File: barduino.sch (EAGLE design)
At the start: 30 parts, among them J1 JACK.65MM, Q2 16MHz

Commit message: Stripped a lot and added some clock parts
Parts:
- removed FTDI: (no value), pinhead:PINHD-1X6
- removed JP1, JP2: (no value), SparkFun:M04PTH
- removed JP3: (no value), SparkFun:M06LOCK
- removed JP4, JP5: (no value), SparkFun:M02LOCK
- removed R5: 0, ng:RESISTOR1206
- removed SCHOTTKY_2: (no value), 01_ng:DIODESOD123
- added LED1: (no value), microbuilder:DISP_SEGMENT_4DIGIT_BL-Q56C43
- added SG1: F/CM12P, buzzer:F/CM12P
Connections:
- removed net CONNECT: FTDI.3, SCHOTTKY_2.A
- new net N$22: LED1.P$6
- new net N$23: LED1.P$7
- new net N$27: LED1.P$11
- net A0: no longer JP1.4
- net A1: no longer JP1.3
- net A2: no longer JP1.2
- net A3: no longer JP1.1
- net D0: now also LED1.P$12; no longer FTDI.4, JP2.4
- net D1: now also LED1.P$8; no longer FTDI.5, JP2.3
- net D10: now also SG1.1; no longer JP3.1
- net D2: now also LED1.P$13; no longer JP2.2
- net D3: now also LED1.P$9; no longer JP2.1
- net D4: now also LED1.P$10
- net D5: no longer JP3.6
- net D6: no longer JP3.5
- net D7: no longer JP3.4
- net D8: no longer JP3.3
- net D9: no longer JP3.2
- net GND: now also SG1.2; no longer FTDI.1, JP4.2, JP5.2
- net RTS#: no longer FTDI.6
- net VCC: no longer JP4.1, JP5.1, SCHOTTKY_2.C
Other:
- note added: "Buzzer"
- moved on the sheet: ICSP

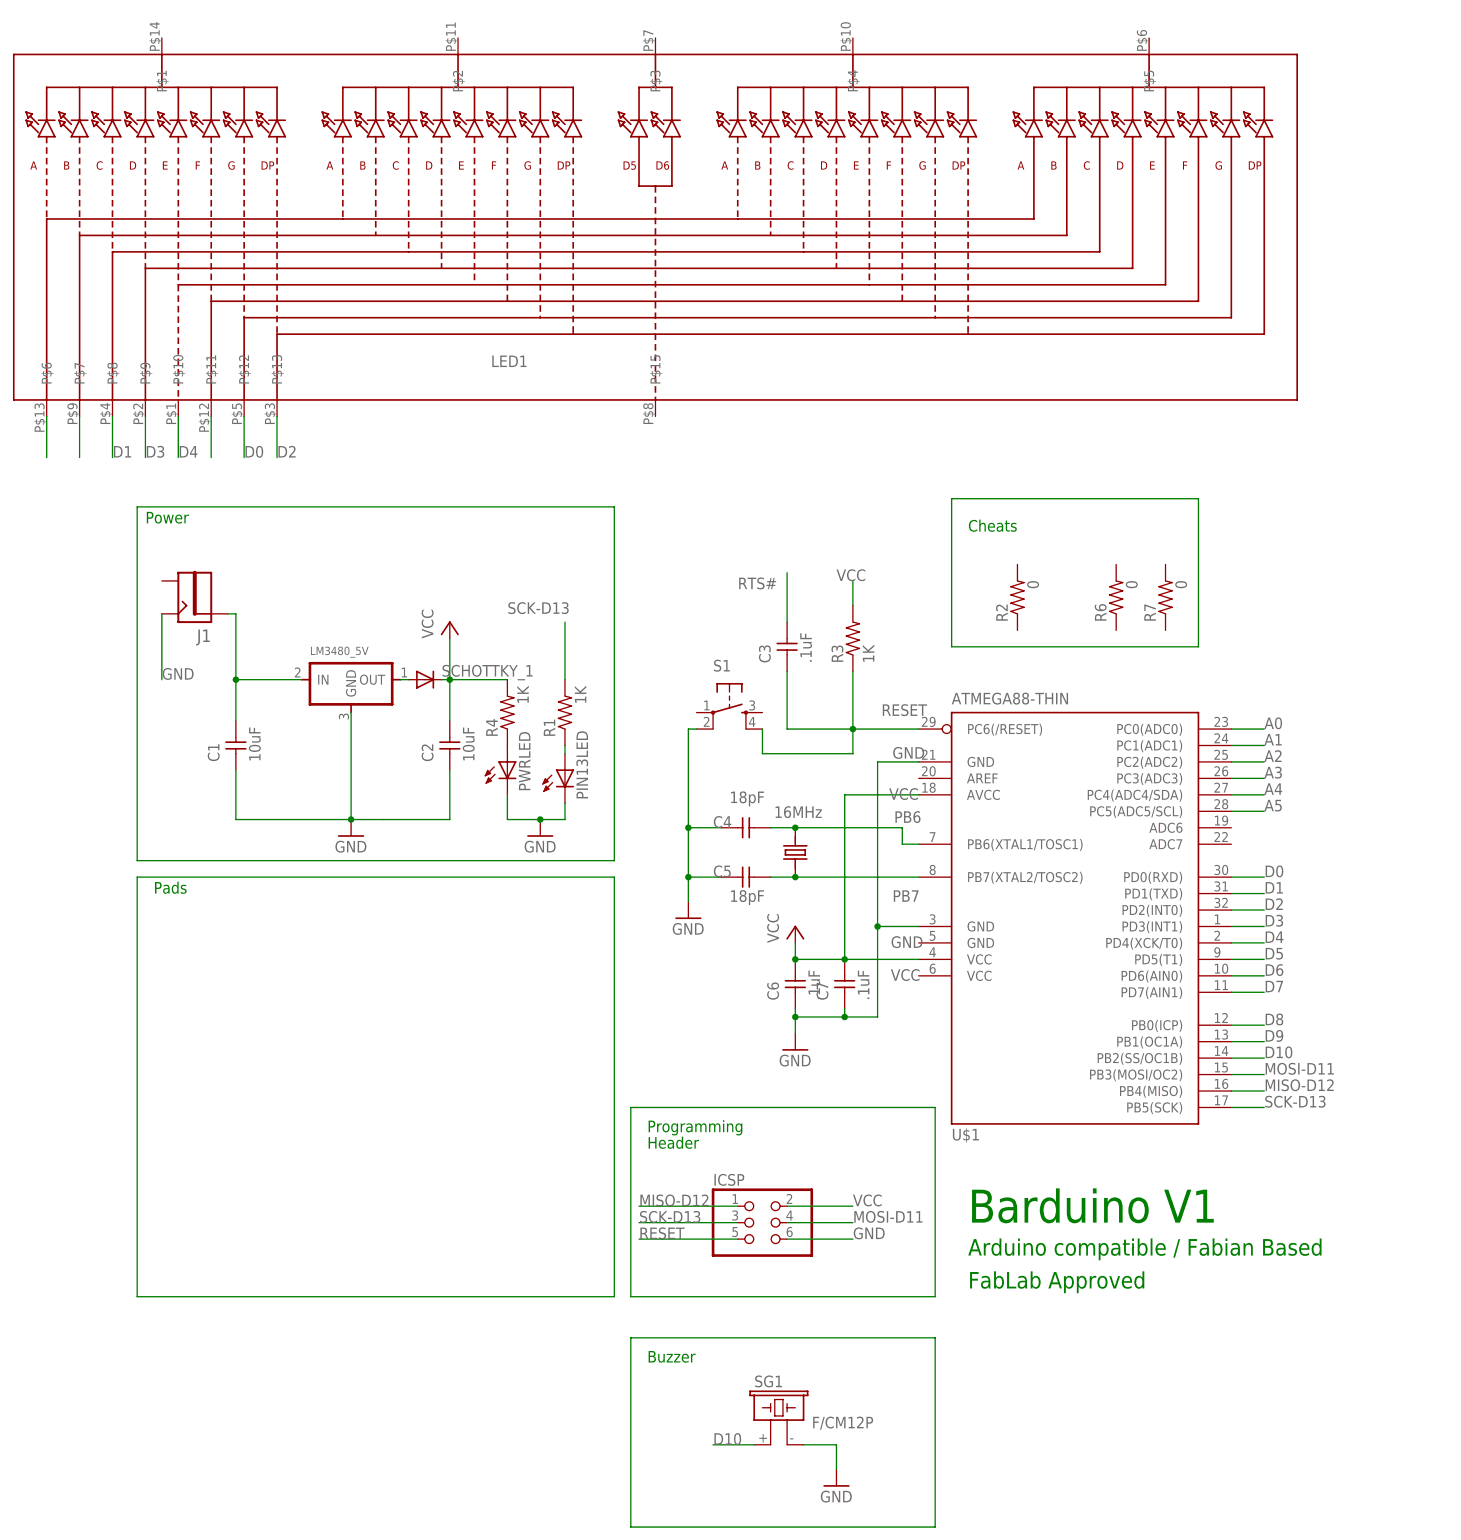
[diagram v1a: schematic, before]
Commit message: Replace pwr jack with usb conn
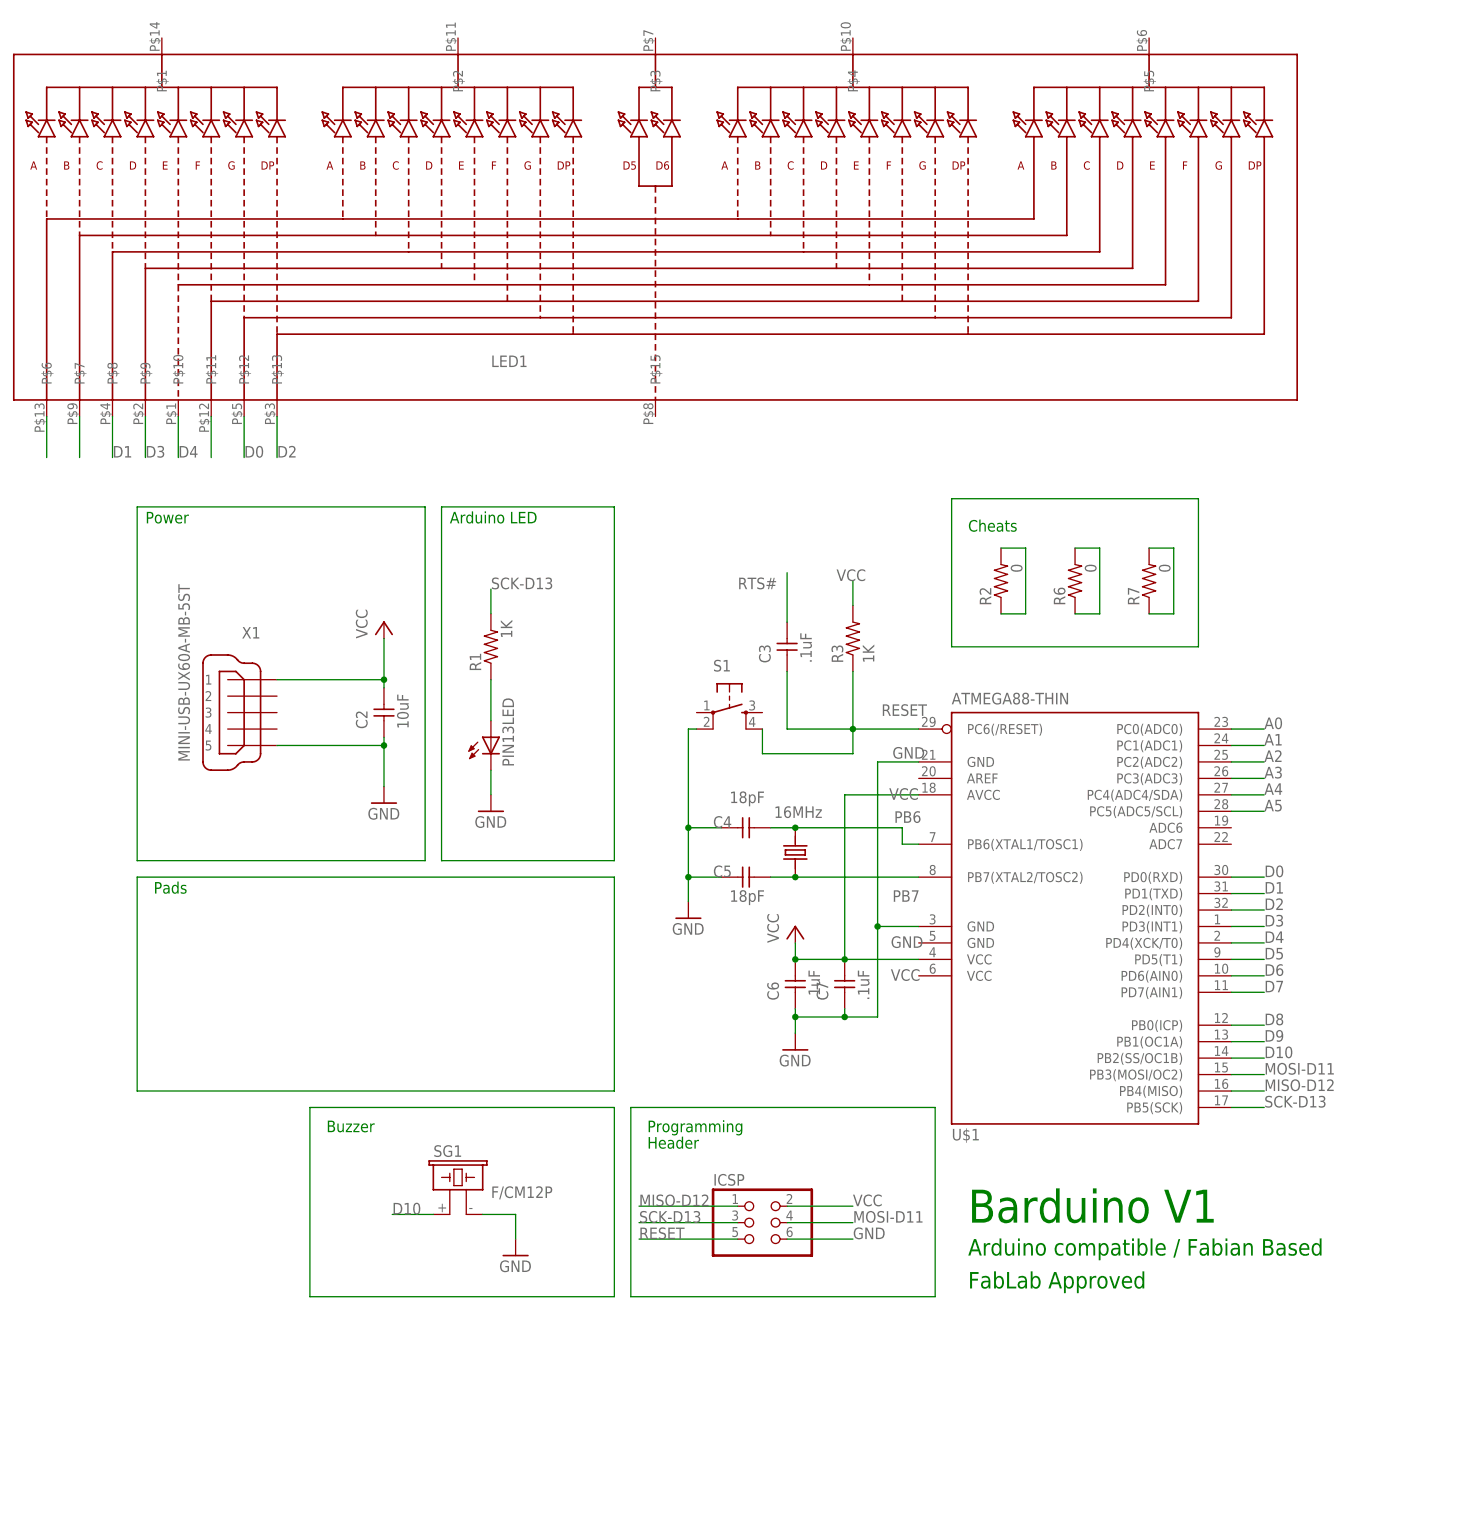
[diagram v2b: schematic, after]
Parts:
- removed C1: 10uF, ng:UNPOLARIZED_CAPACITOR1206
- removed J1: JACK.65MM, ng:JACK.65MM
- removed LM3480_5V: (no value), ng:REGULATORSOT23
- removed PWRLED: (no value), ng:LED1206
- removed R4: 1K, ng:RESISTOR1206
- removed SCHOTTKY_1: (no value), 01_ng:DIODESOD123
- added X1: MINI-USB-UX60A-MB-5ST, con-hirose:MINI-USB-UX60A-MB-5ST
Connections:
- removed net N$1: LM3480_5V.OUT, SCHOTTKY_1.A
- removed net N$2: PWRLED.A, R4.1
- new net N$26: R2.1, R2.2
- net GND: now also X1.5; no longer C1.1, J1.CONTACT, LM3480_5V.GND, PWRLED.C
- net N$3: now also R6.1, R6.2; no longer C1.2, J1.PIN, LM3480_5V.IN
- net VCC: now also R7.1, R7.2, X1.1; no longer R4.2, SCHOTTKY_1.C
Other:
- note added: "Arduino LED"
- moved on the sheet: C2, PIN13LED, R1, R2, R6, R7, SG1

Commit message: clean up a little
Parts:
- removed C3: .1uF, ng:UNPOLARIZED_CAPACITOR1206
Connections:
- removed net RTS#: C3.2
- net RESET: no longer C3.1
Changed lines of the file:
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@@
 <layer number="56" name="wert" color="7" fill="1" visible="no" active="no"/>
 <layer number="57" name="tCAD" color="7" fill="1" visible="no" active="no"/>
+<layer number="90" name="Modules" color="5" fill="1" visible="yes" active="yes"/>
 <layer number="91" name="Nets" color="2" fill="1" visible="yes" active="yes"/>
 <layer number="92" name="Busses" color="1" fill="1" visible="yes" active="yes"/>
@@
 <part name="P+2" library="supply1" deviceset="VCC" device=""/>
 <part name="S1" library="ng" deviceset="6MM_SWITCH" device="6MM_SWITCH"/>
-<part name="C3" library="ng" deviceset="UNPOLARIZED_CAPACITOR" device="1206" value=".1uF"/>
 <part name="R1" library="ng" deviceset="RESISTOR" device="1206" value="1K"/>
 <part name="PIN13LED" library="ng" deviceset="LED" device="1206"/>
@@
 <instance part="P+2" gate="VCC" x="-13.97" y="113.03"/>
 <instance part="S1" gate="2" x="39.37" y="99.06" rot="R270"/>
-<instance part="C3" gate="1" x="48.26" y="110.49" rot="R90"/>
 <instance part="R1" gate="G$1" x="2.54" y="109.22" smashed="yes" rot="R90">
 <attribute name="NAME" x="1.0414" y="105.41" size="1.778" layer="95" rot="R90"/>
@@
 <segment>
 <wire x1="58.42" y1="115.57" x2="58.42" y2="119.38" width="0.1524" layer="91"/>
-<label x="55.88" y="119.38" size="1.778" layer="95"/>
+<label x="58.42" y="119.38" size="1.778" layer="95"/>
 <pinref part="R3" gate="G$1" pin="2"/>
 </segment>
@@
 <segment>
 <wire x1="58.42" y1="96.52" x2="58.42" y2="105.41" width="0.1524" layer="91"/>
-<wire x1="44.45" y1="96.52" x2="44.45" y2="92.71" width="0.1524" layer="91"/>
-<wire x1="44.45" y1="92.71" x2="58.42" y2="92.71" width="0.1524" layer="91"/>
-<wire x1="58.42" y1="92.71" x2="58.42" y2="96.52" width="0.1524" layer="91"/>
+<wire x1="44.45" y1="96.52" x2="58.42" y2="96.52" width="0.1524" layer="91"/>
 <wire x1="68.58" y1="96.52" x2="58.42" y2="96.52" width="0.1524" layer="91"/>
-<wire x1="48.26" y1="105.41" x2="48.26" y2="96.52" width="0.1524" layer="91"/>
-<wire x1="58.42" y1="96.52" x2="48.26" y2="96.52" width="0.1524" layer="91"/>
 <junction x="58.42" y="96.52"/>
 <label x="69.85" y="100.33" size="1.778" layer="95" rot="R180"/>
@@
 <pinref part="S1" gate="2" pin="S1"/>
 <pinref part="U$1" gate="G$1" pin="PC6(/RESET)"/>
-<pinref part="C3" gate="1" pin="1"/>
 </segment>
 <segment>
@@
 </segment>
 </net>
-<net name="RTS#" class="0">
-<segment>
-<wire x1="48.26" y1="113.03" x2="48.26" y2="120.65" width="0.1524" layer="91"/>
-<label x="40.64" y="118.11" size="1.778" layer="95"/>
-<pinref part="C3" gate="1" pin="2"/>
-</segment>
-</net>
 <net name="D1" class="0">
 <segment>
@@
 <wire x1="21.59" y1="38.1" x2="21.59" y2="8.89" width="0.1524" layer="91"/>
 <wire x1="21.59" y1="8.89" x2="-25.4" y2="8.89" width="0.1524" layer="91"/>
-</segment>
-</net>
-<net name="N$1" class="0">
-<segment>
-<wire x1="-5.08" y1="76.2" x2="-5.08" y2="130.81" width="0.1524" layer="91"/>
-<wire x1="-5.08" y1="130.81" x2="21.59" y2="130.81" width="0.1524" layer="91"/>
-<wire x1="21.59" y1="130.81" x2="21.59" y2="76.2" width="0.1524" layer="91"/>
-<wire x1="21.59" y1="76.2" x2="-5.08" y2="76.2" width="0.1524" layer="91"/>
 </segment>
 </net>
@@
 </segment>
 </net>
+<net name="N$1" class="0">
+<segment>
+<wire x1="-5.08" y1="130.81" x2="-5.08" y2="76.2" width="0.1524" layer="91"/>
+<wire x1="-5.08" y1="76.2" x2="21.59" y2="76.2" width="0.1524" layer="91"/>
+<wire x1="21.59" y1="76.2" x2="21.59" y2="130.81" width="0.1524" layer="91"/>
+<wire x1="21.59" y1="130.81" x2="-5.08" y2="130.81" width="0.1524" layer="91"/>
+</segment>
+</net>
